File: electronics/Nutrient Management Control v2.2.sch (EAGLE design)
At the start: 14 parts, among them IC1 7407N, Q1 FQP30N06L

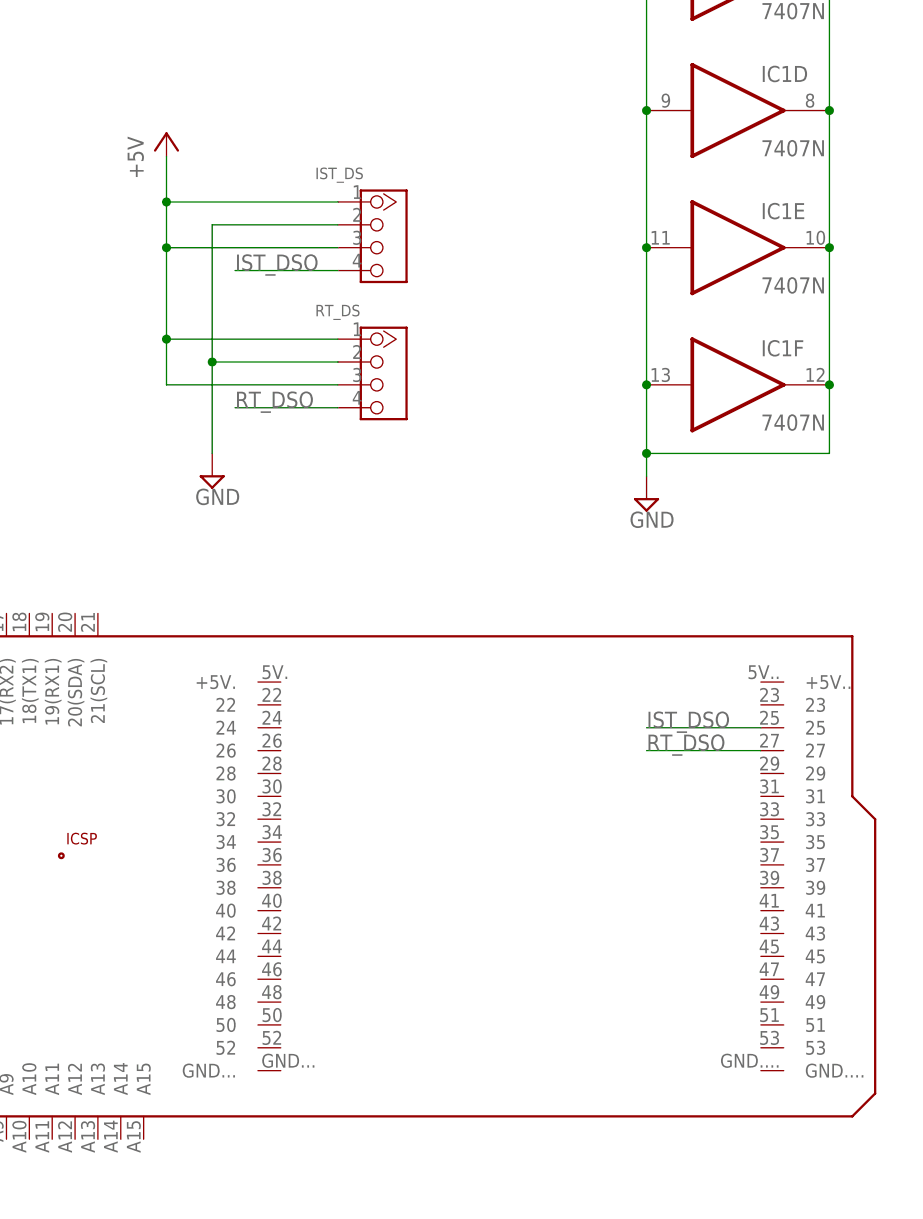
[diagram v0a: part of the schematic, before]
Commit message: Correcting pins, debug and naming conventions
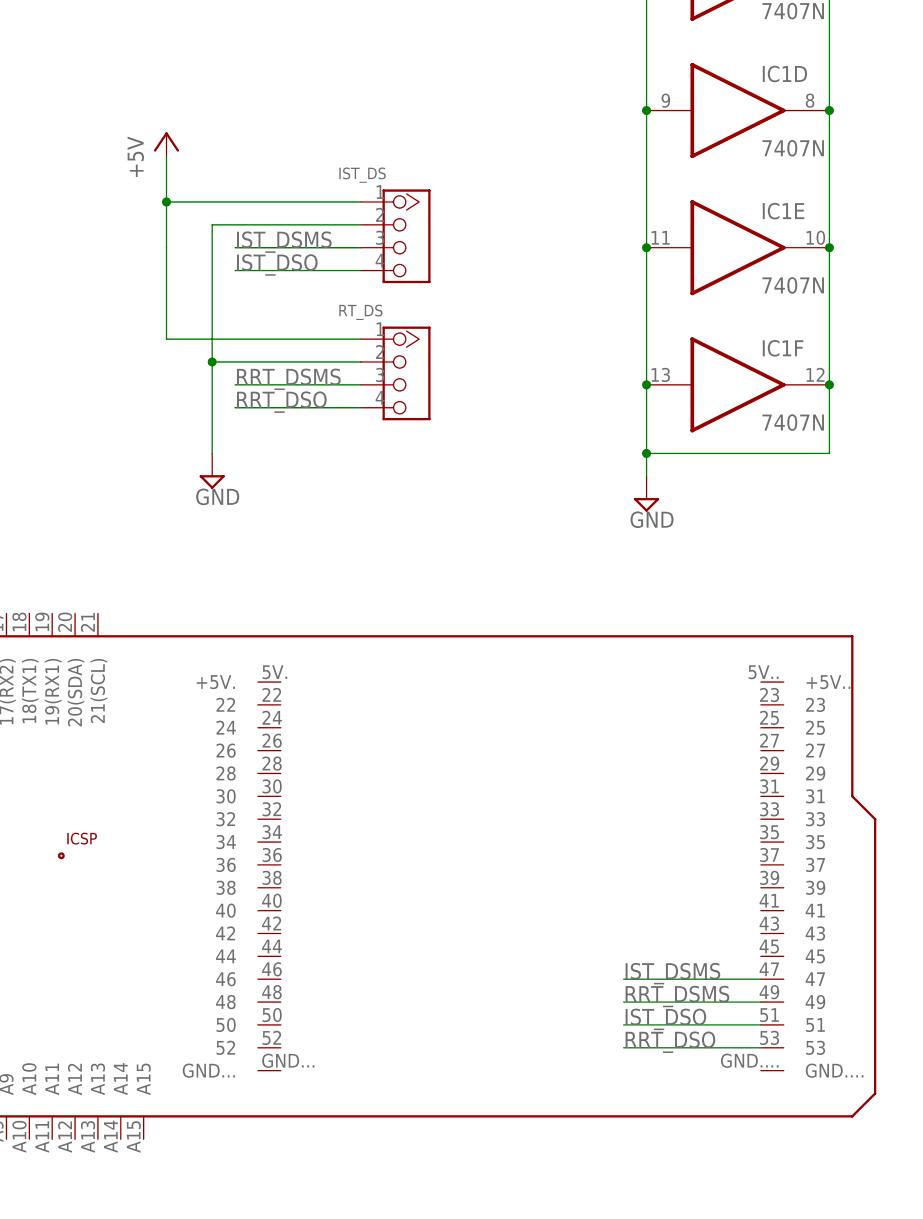
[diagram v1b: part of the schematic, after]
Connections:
- removed net RT_DSO: PCB2.27, RT_DS.4
- new net IST_DSMS: IST_DS.3, PCB2.47
- new net RRT_DSMS: PCB2.49, RT_DS.3
- new net RRT_DSO: PCB2.53, RT_DS.4
- net +5V: no longer IST_DS.3, RT_DS.3
- net IST_DSO: now also PCB2.51; no longer PCB2.25
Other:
- moved on the sheet: IST_DS, RT_DS
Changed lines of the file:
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@@
 <attribute name="VALUE" x="165.1" y="-7.62" size="1.778" layer="96"/>
 </instance>
-<instance part="IST_DS" gate="G$1" x="121.92" y="13.97" smashed="yes">
-<attribute name="NAME" x="115.57" y="20.32" size="1.27" layer="95" ratio="10"/>
-</instance>
-<instance part="RT_DS" gate="G$1" x="121.92" y="-1.27" smashed="yes">
-<attribute name="NAME" x="115.57" y="5.08" size="1.27" layer="95" ratio="10"/>
+<instance part="IST_DS" gate="G$1" x="124.46" y="13.97" smashed="yes">
+<attribute name="NAME" x="118.11" y="20.32" size="1.27" layer="95" ratio="10"/>
+</instance>
+<instance part="RT_DS" gate="G$1" x="124.46" y="-1.27" smashed="yes">
+<attribute name="NAME" x="118.11" y="5.08" size="1.27" layer="95" ratio="10"/>
 </instance>
 <instance part="P+1" gate="1" x="99.06" y="25.4" smashed="yes">
@@
 <segment>
 <pinref part="IST_DS" gate="G$1" pin="1"/>
-<wire x1="118.11" y1="17.78" x2="99.06" y2="17.78" width="0.1524" layer="91"/>
+<wire x1="120.65" y1="17.78" x2="99.06" y2="17.78" width="0.1524" layer="91"/>
 <pinref part="P+1" gate="1" pin="+5V"/>
 <wire x1="99.06" y1="17.78" x2="99.06" y2="22.86" width="0.1524" layer="91"/>
 <pinref part="RT_DS" gate="G$1" pin="1"/>
-<wire x1="118.11" y1="2.54" x2="99.06" y2="2.54" width="0.1524" layer="91"/>
+<wire x1="120.65" y1="2.54" x2="99.06" y2="2.54" width="0.1524" layer="91"/>
 <wire x1="99.06" y1="2.54" x2="99.06" y2="12.7" width="0.1524" layer="91"/>
 <junction x="99.06" y="17.78"/>
-<pinref part="IST_DS" gate="G$1" pin="3"/>
 <wire x1="99.06" y1="12.7" x2="99.06" y2="17.78" width="0.1524" layer="91"/>
-<wire x1="118.11" y1="12.7" x2="99.06" y2="12.7" width="0.1524" layer="91"/>
-<junction x="99.06" y="12.7"/>
-<pinref part="RT_DS" gate="G$1" pin="3"/>
-<wire x1="118.11" y1="-2.54" x2="99.06" y2="-2.54" width="0.1524" layer="91"/>
-<wire x1="99.06" y1="-2.54" x2="99.06" y2="2.54" width="0.1524" layer="91"/>
-<junction x="99.06" y="2.54"/>
 </segment>
 </net>
@@
 <segment>
 <pinref part="IST_DS" gate="G$1" pin="2"/>
-<wire x1="118.11" y1="15.24" x2="104.14" y2="15.24" width="0.1524" layer="91"/>
+<wire x1="120.65" y1="15.24" x2="104.14" y2="15.24" width="0.1524" layer="91"/>
 <pinref part="SUPPLY2" gate="GND" pin="GND"/>
 <wire x1="104.14" y1="15.24" x2="104.14" y2="0" width="0.1524" layer="91"/>
 <pinref part="RT_DS" gate="G$1" pin="2"/>
 <wire x1="104.14" y1="0" x2="104.14" y2="-10.16" width="0.1524" layer="91"/>
-<wire x1="118.11" y1="0" x2="104.14" y2="0" width="0.1524" layer="91"/>
+<wire x1="120.65" y1="0" x2="104.14" y2="0" width="0.1524" layer="91"/>
 <junction x="104.14" y="0"/>
 </segment>
@@
 <segment>
 <pinref part="IST_DS" gate="G$1" pin="4"/>
-<wire x1="118.11" y1="10.16" x2="106.68" y2="10.16" width="0.1524" layer="91"/>
+<wire x1="120.65" y1="10.16" x2="106.68" y2="10.16" width="0.1524" layer="91"/>
 <label x="106.68" y="10.16" size="1.778" layer="95"/>
 </segment>
 <segment>
-<pinref part="PCB2" gate="G$1" pin="25"/>
-<wire x1="165.1" y1="-40.64" x2="152.4" y2="-40.64" width="0.1524" layer="91"/>
-<label x="152.4" y="-40.64" size="1.778" layer="95"/>
-</segment>
-</net>
-<net name="RT_DSO" class="0">
+<pinref part="PCB2" gate="G$1" pin="51"/>
+<wire x1="165.1" y1="-73.66" x2="149.86" y2="-73.66" width="0.1524" layer="91"/>
+<label x="149.86" y="-73.66" size="1.778" layer="95"/>
+</segment>
+</net>
+<net name="RRT_DSO" class="0">
 <segment>
 <pinref part="RT_DS" gate="G$1" pin="4"/>
-<wire x1="118.11" y1="-5.08" x2="106.68" y2="-5.08" width="0.1524" layer="91"/>
+<wire x1="120.65" y1="-5.08" x2="106.68" y2="-5.08" width="0.1524" layer="91"/>
 <label x="106.68" y="-5.08" size="1.778" layer="95"/>
 </segment>
 <segment>
-<pinref part="PCB2" gate="G$1" pin="27"/>
-<wire x1="165.1" y1="-43.18" x2="152.4" y2="-43.18" width="0.1524" layer="91"/>
-<label x="152.4" y="-43.18" size="1.778" layer="95"/>
-</segment>
-</net>
+<pinref part="PCB2" gate="G$1" pin="53"/>
+<wire x1="165.1" y1="-76.2" x2="149.86" y2="-76.2" width="0.1524" layer="91"/>
+<label x="149.86" y="-76.2" size="1.778" layer="95"/>
+</segment>
+</net>
+<net name="IST_DSMS" class="0">
+<segment>
+<pinref part="IST_DS" gate="G$1" pin="3"/>
+<wire x1="120.65" y1="12.7" x2="106.68" y2="12.7" width="0.1524" layer="91"/>
+<label x="106.68" y="12.7" size="1.778" layer="95"/>
+</segment>
+<segment>
+<pinref part="PCB2" gate="G$1" pin="47"/>
+<wire x1="165.1" y1="-68.58" x2="149.86" y2="-68.58" width="0.1524" layer="91"/>
+<label x="149.86" y="-68.58" size="1.778" layer="95"/>
+</segment>
+</net>
+<net name="RRT_DSMS" class="0">
+<segment>
+<pinref part="RT_DS" gate="G$1" pin="3"/>
+<wire x1="120.65" y1="-2.54" x2="106.68" y2="-2.54" width="0.1524" layer="91"/>
+<label x="106.68" y="-2.54" size="1.778" layer="95"/>
+</segment>
+<segment>
+<pinref part="PCB2" gate="G$1" pin="49"/>
+<wire x1="165.1" y1="-71.12" x2="149.86" y2="-71.12" width="0.1524" layer="91"/>
+<label x="149.86" y="-71.12" size="1.778" layer="95"/>
+</segment>
+</net>

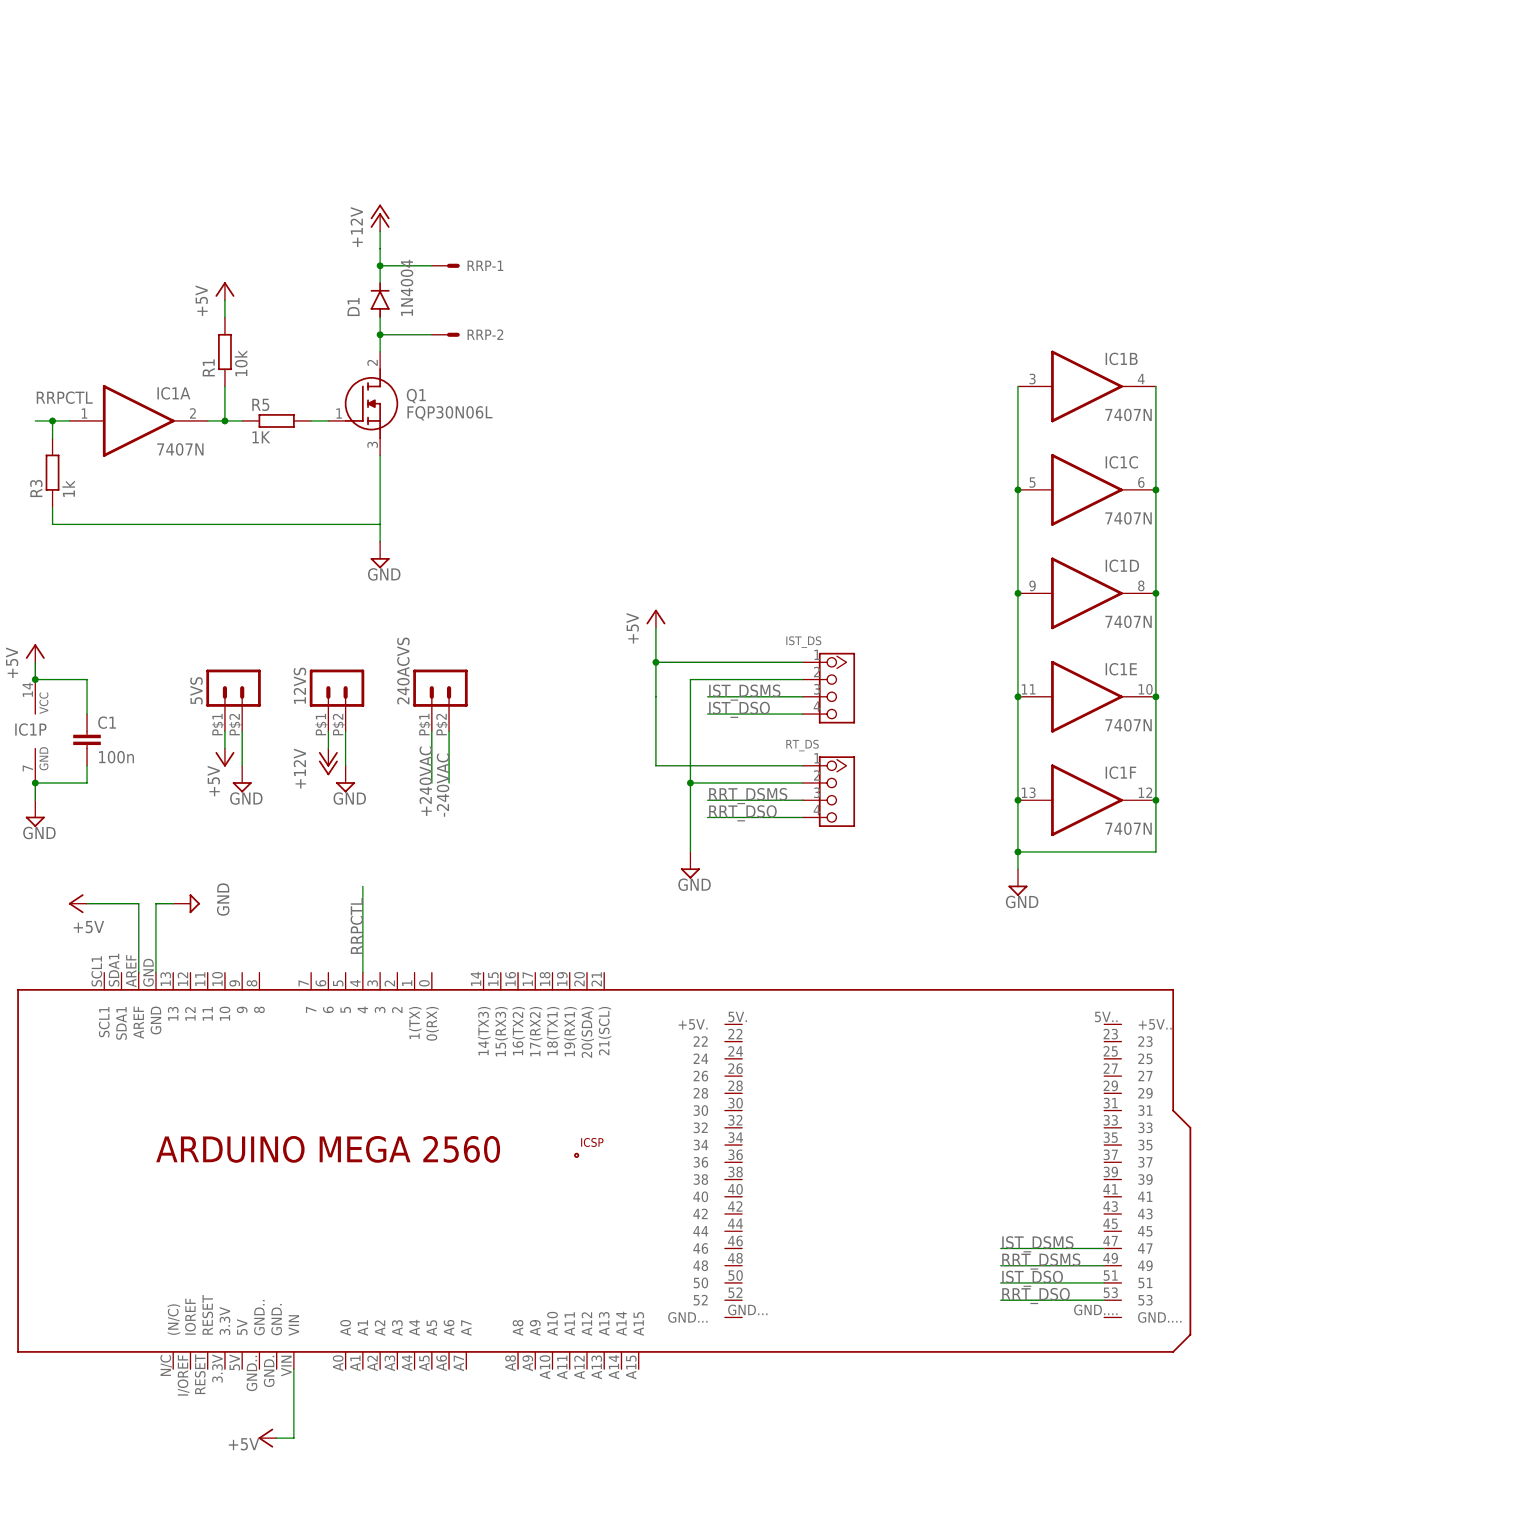
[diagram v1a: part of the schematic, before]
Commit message: First cut of Nutrient Management with multi UART breakout boards
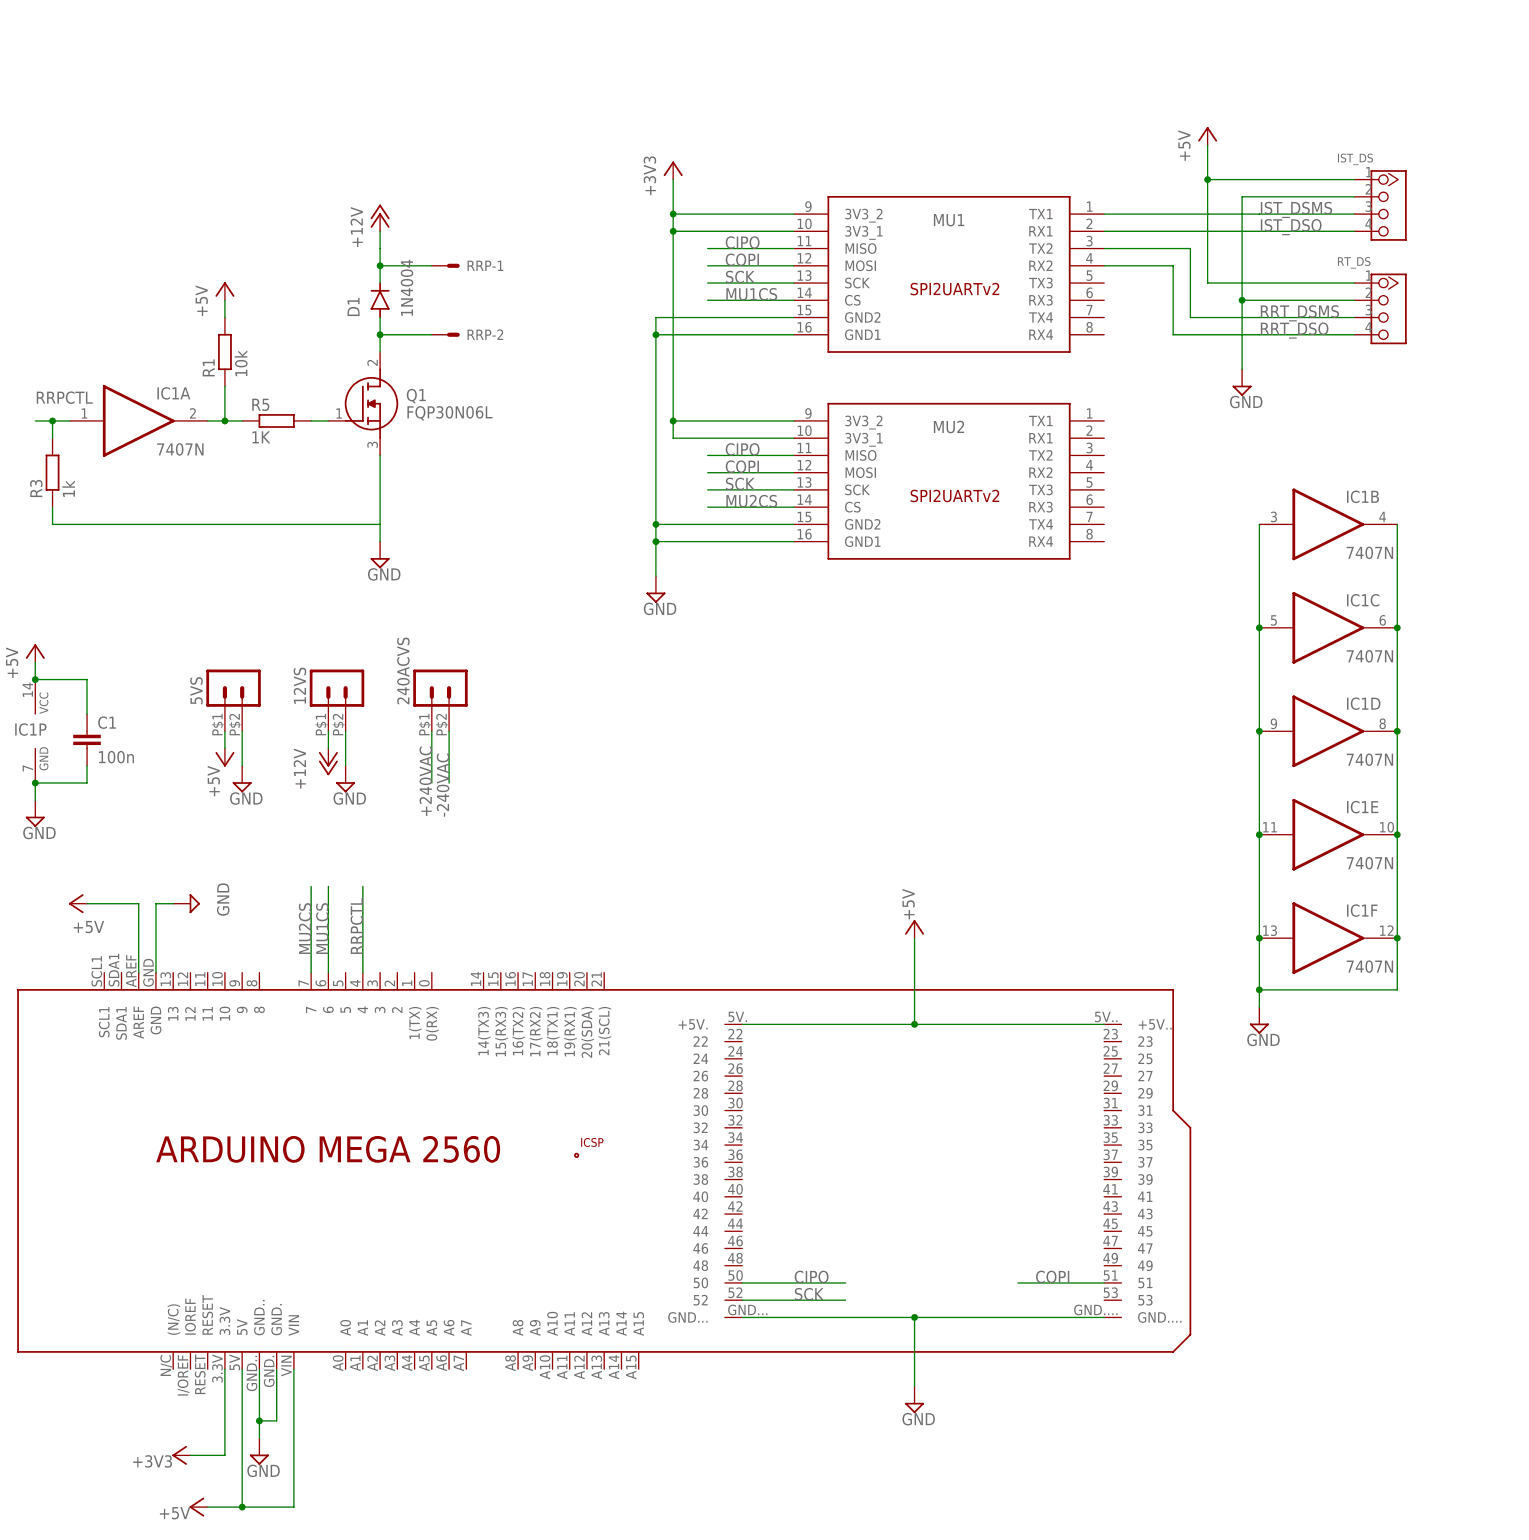
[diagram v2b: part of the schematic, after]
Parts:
- added MU1, MU2: SPI2UART_HEADERS, Aeroponics Control:SPI2UART_HEADERS
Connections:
- new net +3V3: MU1.3V3_1, MU1.3V3_2, MU2.3V3_1, MU2.3V3_2, PCB2.3.3V
- new net CIPO: MU1.MISO, MU2.MISO, PCB2.50
- new net COPI: MU1.MOSI, MU2.MOSI, PCB2.51
- new net MU1CS: MU1.CS, PCB2.6
- new net MU2CS: MU2.CS, PCB2.7
- new net SCK: MU1.SCK, MU2.SCK, PCB2.52
- net +5V: now also PCB2.+5V., PCB2.+5V.., PCB2.5V
- net GND: now also MU1.GND1, MU1.GND2, MU2.GND1, MU2.GND2, PCB2.GND., PCB2.GND.., PCB2.GND..., PCB2.GND....
- net IST_DSMS: now also MU1.TX1; no longer PCB2.47
- net IST_DSO: now also MU1.RX1; no longer PCB2.51
- net RRT_DSMS: now also MU1.TX2; no longer PCB2.49
- net RRT_DSO: now also MU1.RX2; no longer PCB2.53
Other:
- moved on the sheet: IC1B, IC1C, IC1D, IC1E, IC1F, IST_DS, RT_DS
